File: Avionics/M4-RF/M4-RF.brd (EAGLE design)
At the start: 50.8 x 50.5 mm, 25 parts, among them J1 132134RP, U1 CC1120, U2 CC1190, U3 CC2520, U4 CC2592, U5 INF-PG-LQFP-100-11-7000X7000E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

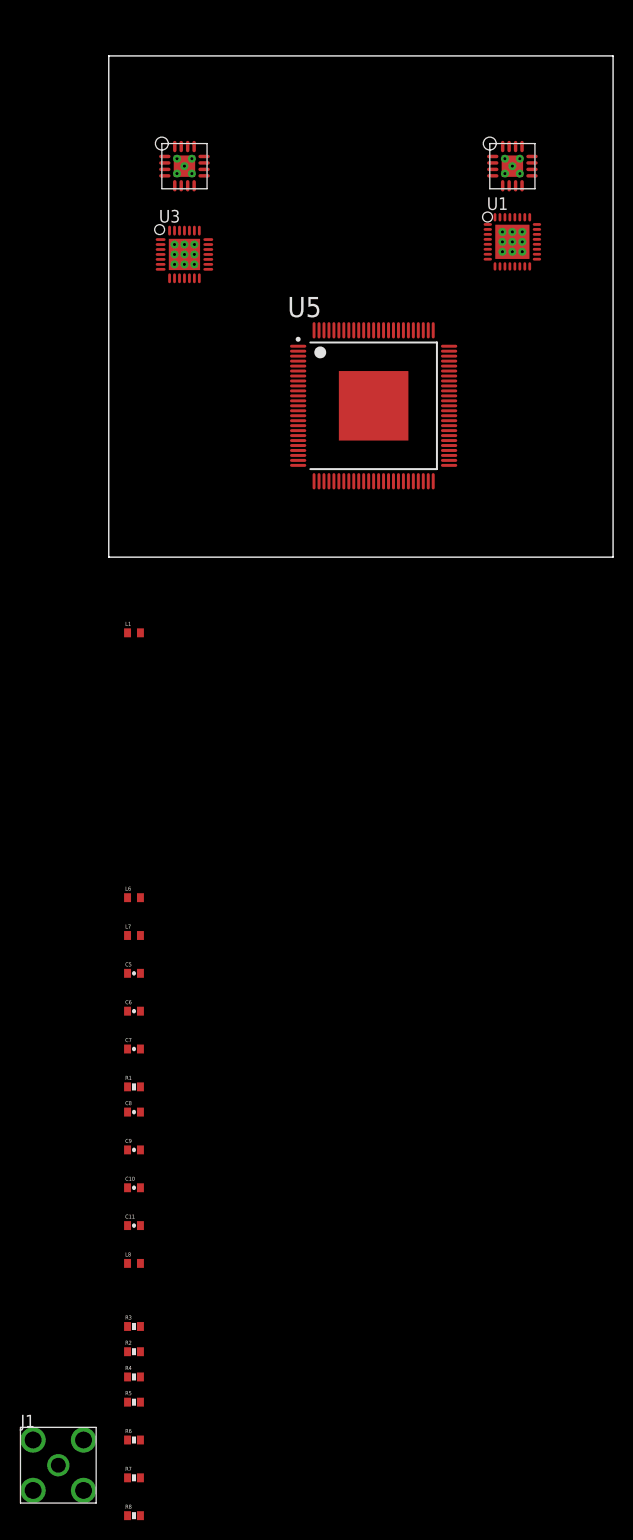
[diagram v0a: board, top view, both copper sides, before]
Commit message: Fixed library references and added balun to 2.4GHz circuit
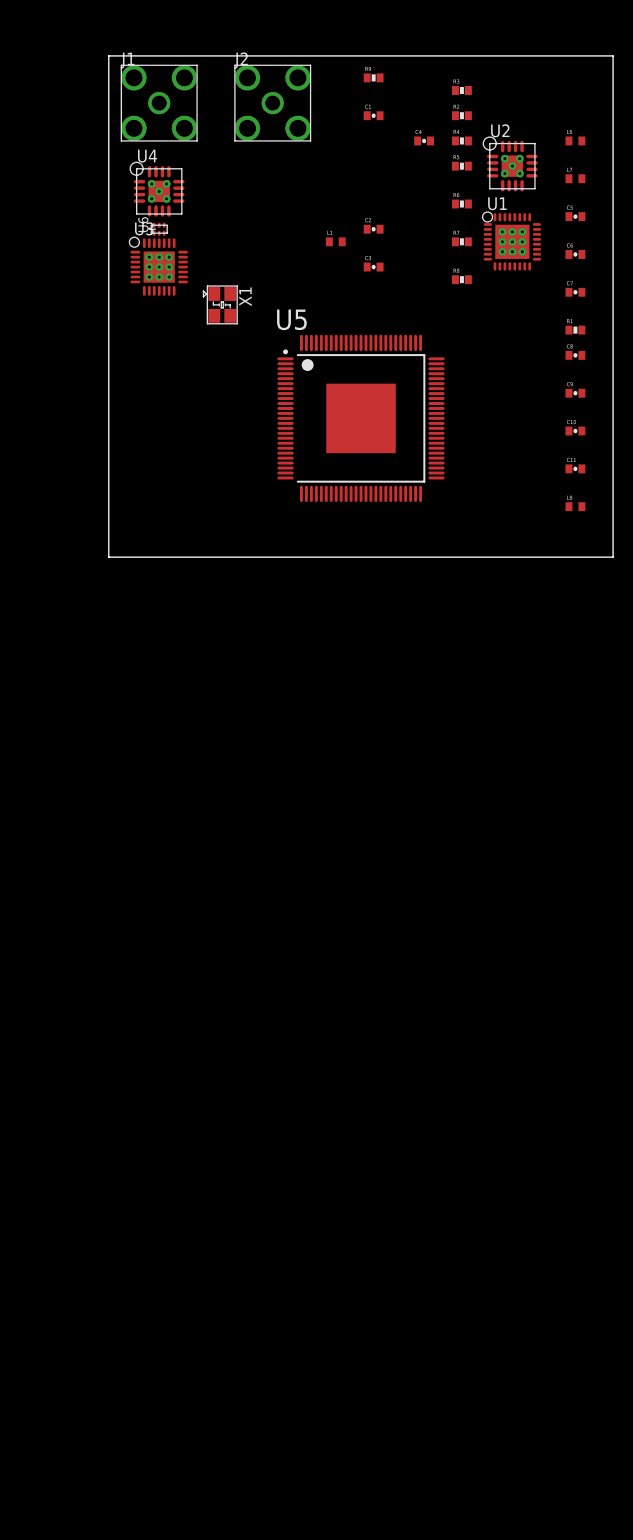
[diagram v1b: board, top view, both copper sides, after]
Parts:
- added C1: 0.1u, SparkFun-Capacitors:0402-CAP
- added C2, C3: 12p, SparkFun-Capacitors:0402-CAP
- added C4: 6.8p, SparkFun-Capacitors:0402-CAP
- added J2: 132134RP, connectors:RP-SMA-TH
- added R9: 56k, SparkFun-Resistors:0402-RES
- added U6: LDB182G4520C-110, rf:LDB18
- added X1: NX3225SA-32MHZ-EXS00A-CS0236832MHZ, oscillators:OSC-4-SMD-3.2MMX2.5MM
- U1: device ti_rf:RHB_S-PVQFN-N32 -> rf:RHB_S-PVQFN-N32
- U2, U4: device ti_rf:RGV_S-PVGFN-N16 -> rf:RGV_S-PVQFN-N16
- U3: device ti_rf:RHD_S-PVQFN-N28 -> rf:RHD_S-PVQFN-N28
- moved J1 137.5 mm to (5.08, 45.7)
- moved R2 128.8 mm to (35.6, 44.5)
- moved R3 128.8 mm to (35.6, 47.0)
- moved R4 128.8 mm to (35.6, 41.9)
- moved R5 128.8 mm to (35.6, 39.4)
- moved R6 128.8 mm to (35.6, 35.6)
- moved R7 128.8 mm to (35.6, 31.8)
- moved R8 128.8 mm to (35.6, 27.9)
- moved C10 88.2 mm to (47.0, 12.7)
- moved C11 88.2 mm to (47.0, 8.89)
- moved C6 88.2 mm to (47.0, 30.5)
- moved C7 88.2 mm to (47.0, 26.7)
- moved C8 88.2 mm to (47.0, 20.3)
- moved C9 88.2 mm to (47.0, 16.5)
- moved L7 88.2 mm to (47.0, 38.1)
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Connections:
- net N$12 renamed 2G4_HG
- new net 2G4_LP: J2.P$1
- new net N$14: U3.11, U3.14, U3.16, U3.20, U3.22, U3.24, U3.8
- new net N$15: C2.2, U3.12, X1.1
- new net N$16: R9.1, U3.23
- new net N$17: C1.2, U3.27
- new net N$18: C3.2, U3.13, X1.3
- new net N$19: R4.1, U6.4
- new net N$20: R5.2, U6.6
- new net N$21: U6.1
- new net N$22: C4.1, U6.3
- net GND: now also C1.1, C2.1, C3.1, C4.2, J2.M1, J2.M2, J2.M3, J2.M4, R9.2, U3.4, U3.EXP@10, U3.EXP@11, X1.2, X1.4

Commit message: Applied DRU
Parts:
- removed J2: 132134RP, connectors:RP-SMA-TH
- added R10: DNP, SparkFun-Resistors:0402-RES
- moved R3 31.6 mm to (8.13, 31.2), turned to 90 degrees
- moved R5 29.8 mm to (6.86, 31.2), turned to 90 degrees
- moved R2 29.1 mm to (9.65, 31.2), turned to 90 degrees
- moved R4 26.8 mm to (10.9, 31.2), turned to 270 degrees
- moved R9 14.5 mm to (23.9, 34.0)
- moved L1 14.0 mm to (8.89, 33.0)
- moved X1 4.38 mm to (12.2, 21.1), turned to 0 degrees
- moved U4 3.81 mm to (8.89, 36.8), turned to 90 degrees
- moved U5 3.81 mm to (25.4, 10.2)
- moved U3 3.54 mm to (6.35, 25.9)
- moved U6 0.76 mm to (5.08, 33.8), flipped to the bottom, turned to 270 degrees
- moved J1 0.25 mm to (4.83, 45.7)
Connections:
- removed net N$21: U6.1
- net 2G4_HG: now also R10.2
- net 2G4_LP: now also R10.1, U6.1; no longer J2.P$1
- net GND: now also U1.EP, U1.EXP@1, U1.EXP@2, U1.EXP@3, U1.EXP@4, U1.EXP@5, U1.EXP@6, U1.EXP@7, U1.EXP@8, U1.EXP@9, U2.1, U2.12, U2.3, U2.9, U2.EP, U2.EP@1, U2.EP@2, U2.EP@3, U2.EP@4, U2.EP@5; no longer J2.M1, J2.M2, J2.M3, J2.M4, U3.EXP@10, U3.EXP@11

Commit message: Added more updates to board layout.
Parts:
- removed L1: DNP, SparkFun-Passives:C0402
- removed R4, R5: DNP, SparkFun-Resistors:0402-RES
- R2: value 0 -> RESISTOR-3PIN-LH-0402; device SparkFun-Resistors:0402-RES -> SparkFun-Resistors:0402-RES-3PIN-LH
- R3: value 0 -> RESISTOR-3PIN-RH-0402; device SparkFun-Resistors:0402-RES -> SparkFun-Resistors:0402-RES-3PIN-RH
- X1: value NX3225SA-32MHZ-EXS00A-CS0236832MHZ -> FA-20H32.0000MF20X-K3; device oscillators:OSC-4-SMD-3.2MMX2.5MM -> oscillators:FA-20H
- moved L8 49.0 mm to (10.9, 38.2), turned to 270 degrees
- moved C6 43.7 mm to (4.50, 40.6), turned to 90 degrees
- moved C11 41.8 mm to (14.9, 35.7), turned to 90 degrees
- moved C5 41.7 mm to (5.59, 39.3), turned to 90 degrees
- moved C10 40.7 mm to (13.4, 35.8), turned to 90 degrees
- moved C8 40.4 mm to (12.0, 40.6), turned to 270 degrees
- moved C7 40.2 mm to (8.78, 39.3), turned to 270 degrees
- moved C9 40.0 mm to (11.9, 35.8), turned to 90 degrees
- moved L7 39.8 mm to (7.19, 40.0), turned to 180 degrees
- moved L6 36.6 mm to (10.4, 39.9), turned to 180 degrees
- moved X1 25.7 mm to (22.9, 44.5), turned to 180 degrees
- moved U3 22.0 mm to (23.6, 39.5), turned to 180 degrees
- moved C3 16.4 mm to (20.4, 44.4), turned to 270 degrees
- moved U6 14.4 mm to (18.2, 39.6), turned to 180 degrees
- moved C4 13.9 mm to (17.9, 41.9), flipped to the bottom, turned to 90 degrees
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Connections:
- removed net N$4: L1.1, R3.2, U4.2
- new net N$12: R3.1, U4.2
- net N$1: now also R3.2; no longer R3.1, R5.1
- net N$19: now also R2.3; no longer R4.1
- net N$2: now also R2.2; no longer R2.1, R4.2
- net N$20: now also R3.3; no longer R5.2
- net N$6: now also R2.1; no longer L1.2, R2.2

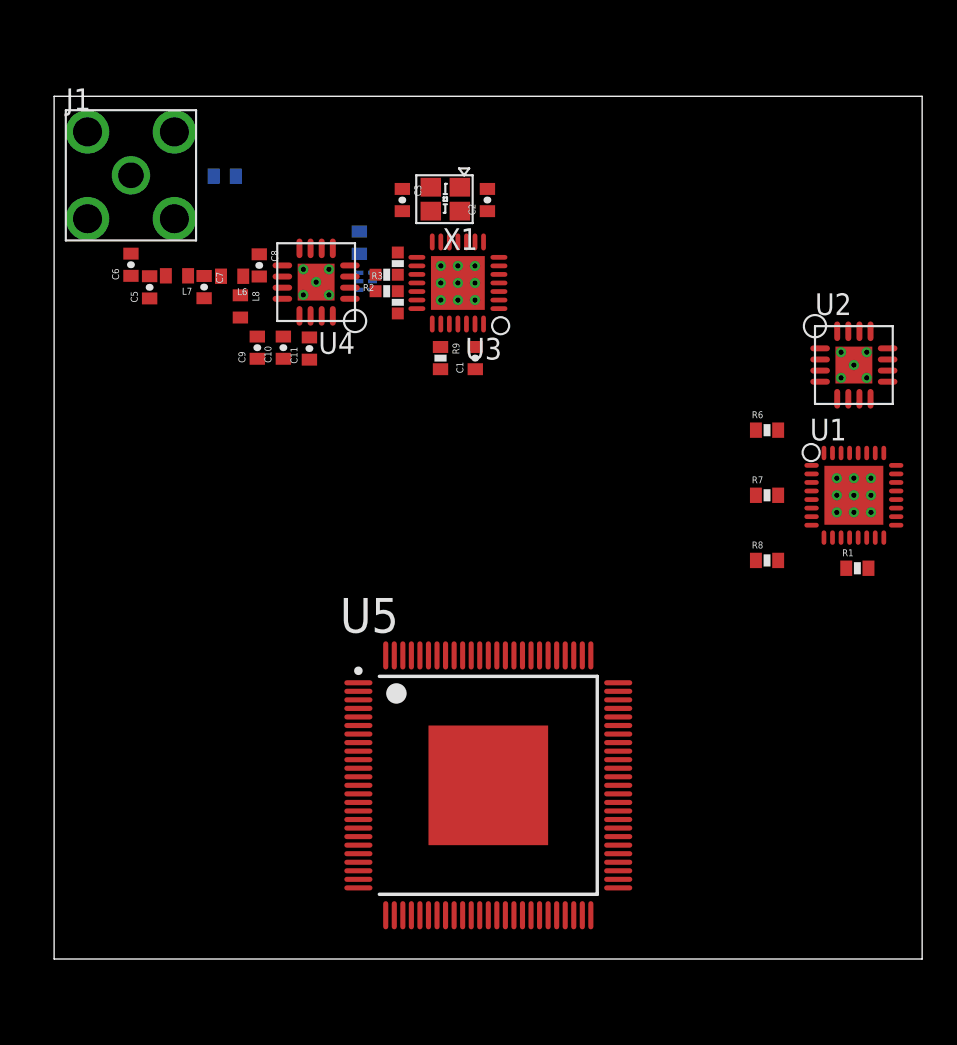
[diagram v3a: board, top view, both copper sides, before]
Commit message: Finished first draft of 2.4GHz layout.
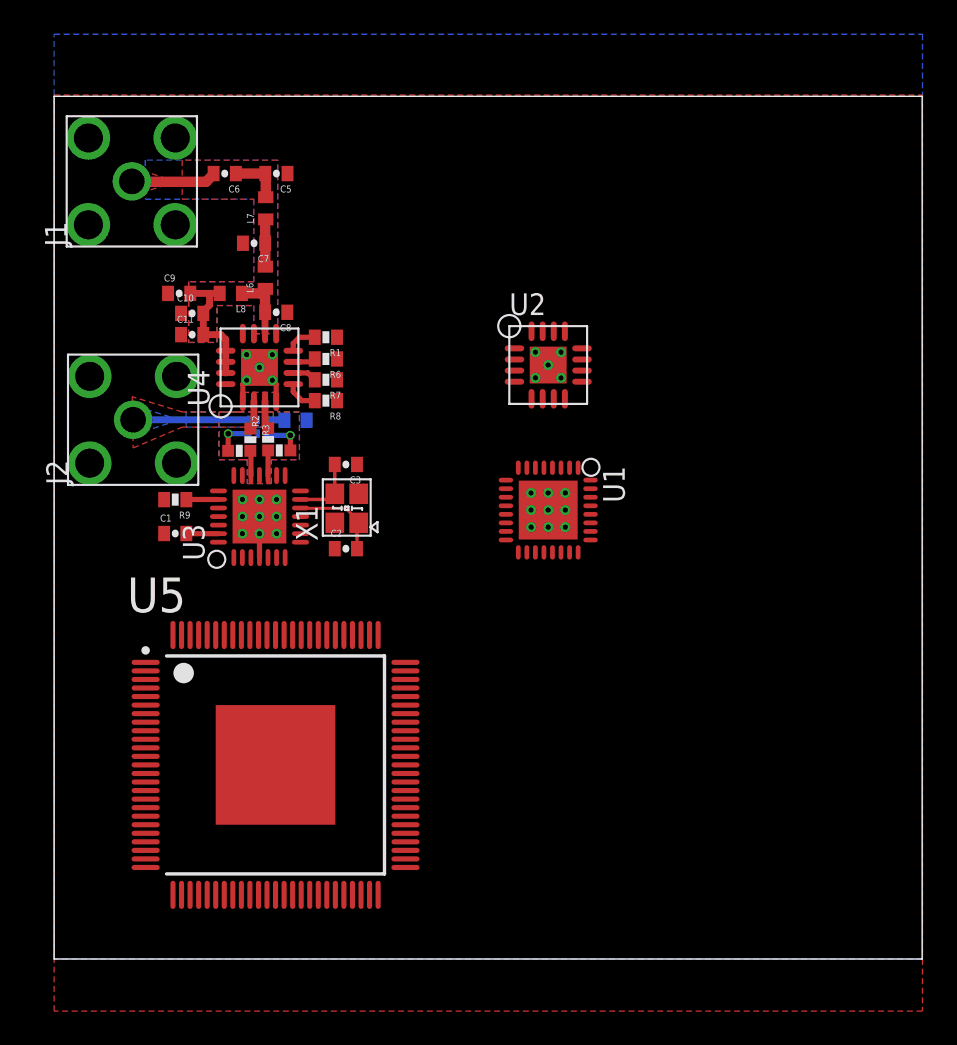
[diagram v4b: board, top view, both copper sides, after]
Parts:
- removed R10: DNP, SparkFun-Resistors:0402-RES
- added J2: 132134RP, connectors:RP-SMA-TH
- moved R1 33.9 mm to (15.9, 36.4), turned to 180 degrees
- moved R8 27.4 mm to (15.9, 32.7), turned to 180 degrees
- moved R7 26.7 mm to (15.9, 33.9), turned to 180 degrees
- moved R6 26.1 mm to (15.9, 35.1), turned to 180 degrees
- moved C2 22.0 mm to (17.1, 24.0), turned to 0 degrees
- moved C1 20.3 mm to (7.09, 24.9), turned to 0 degrees
- moved X1 19.0 mm to (17.1, 26.4), turned to 90 degrees
- moved U3 17.9 mm to (12.0, 25.9), turned to 90 degrees
- moved U1 17.9 mm to (28.9, 26.3), turned to 270 degrees
- moved U2 17.9 mm to (28.9, 34.7)
- moved R9 17.6 mm to (7.09, 26.9), turned to 180 degrees
- moved C3 15.8 mm to (17.1, 28.9), turned to 180 degrees
- moved U5 12.5 mm to (13.0, 11.4)
- moved R2 11.9 mm to (12.5, 30.4), turned to 270 degrees
- moved R3 11.8 mm to (11.5, 30.4), turned to 270 degrees
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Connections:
- removed net 2G4_HG: C6.2, J1.P$1, R10.2
- new net 2G4_LG: C6.2, J1.P$1
- net 2G4_LP: now also J2.P$1; no longer R10.1
- net GND: now also J2.M1, J2.M2, J2.M3, J2.M4
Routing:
- net N$10: track 0.00 -> 7.67 mm
- net 2G4_LP: track 0.00 -> 6.79 mm
- net N$15: track 0.00 -> 5.40 mm
- net 2G4_LG: track 0.00 -> 5.02 mm
- net N$7: track 0.00 -> 4.11 mm
- net GND: track 0.00 -> 4.04 mm
- net N$18: track 0.00 -> 3.85 mm
- net N$9: track 0.00 -> 3.12 mm
- net N$8: track 0.00 -> 2.78 mm
- net N$19: track 0.00 -> 2.32 mm, vias 0 -> 1
- net N$20: track 0.00 -> 2.24 mm, vias 0 -> 1
- net N$13: track 0.00 -> 1.93 mm
- net N$17: track 0.00 -> 1.88 mm
- net N$16: track 0.00 -> 1.88 mm
- net N$11: track 0.00 -> 1.84 mm
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- added copper zone on layer 1, net 2G4_LG
- added copper zone on layer 16, net 2G4_LP
- added copper zone on layer 1, net GND
- added copper zone on layer 15, net GND
- added copper zone on layer 16, net GND
- added copper zone on layer 2, net GND
- added copper zone on layer 1, net N$21
- added copper zone on layer 15, net N$21
- added copper zone on layer 16, net N$21
- added copper zone on layer 2, net N$21
- added copper zone on layer 1, net N$4
- added copper zone on layer 15, net N$4
- added copper zone on layer 16, net N$4
- added copper zone on layer 2, net N$4
- added copper zone on layer 1, net RFCUTOUT1
- added copper zone on layer 15, net RFCUTOUT1
- added copper zone on layer 16, net RFCUTOUT1
- added copper zone on layer 2, net RFCUTOUT1

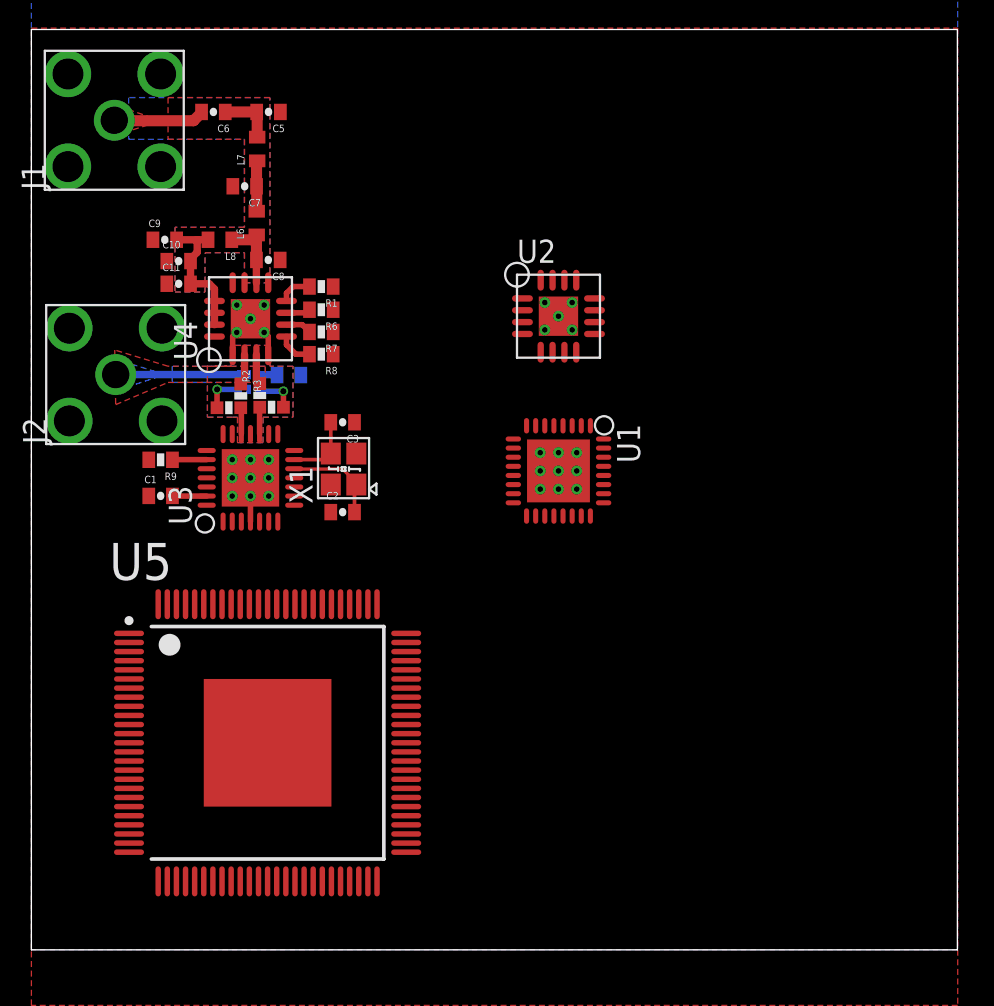
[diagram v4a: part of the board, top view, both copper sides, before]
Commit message: Started to build 900MHz circuit
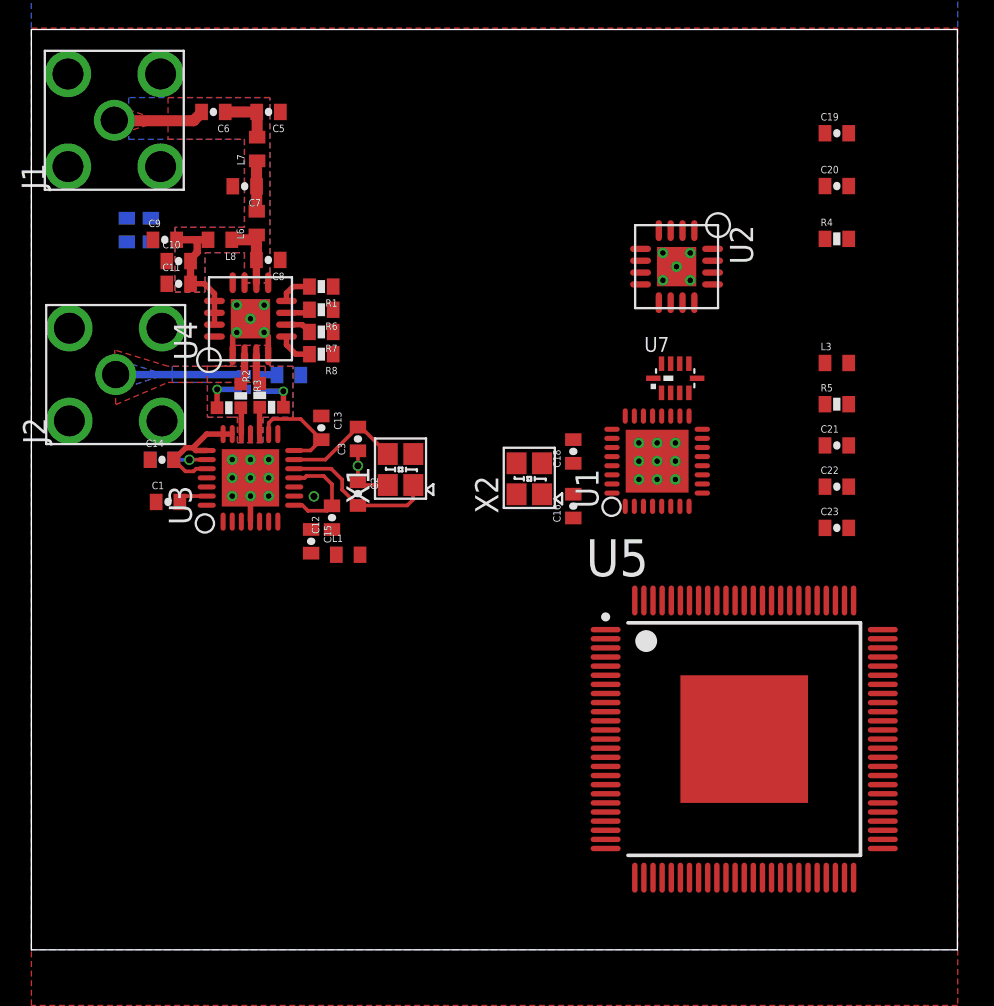
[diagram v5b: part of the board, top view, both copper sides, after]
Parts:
- added C12, C13, C14: 0.1u, SparkFun-Capacitors:0402-CAP
- added C15, C17: 2.2u, SparkFun-Capacitors:0402-CAP
- added C16, C18: 12p, SparkFun-Capacitors:0402-CAP
- added C19: 47n, SparkFun-Capacitors:0402-CAP
- added C20: 220n, SparkFun-Capacitors:0402-CAP
- added C21: 33p, SparkFun-Passives:0402-CAP
- added C22: 10n, SparkFun-Passives:0402-CAP
- added C23: 100p, SparkFun-Passives:0402-CAP
- added L1, L2: BEAD 100, SparkFun-Passives:C0402
- added L3: 10n, SparkFun-Passives:C0402
- added R4: 56k, SparkFun-Resistors:0402-RES
- added R5: 15, SparkFun-Resistors:0402-RES
- added U7: 0900PC15J0013, rf:0900PC15J0013
- added X2: FA-20H32.0000MF20X-K3, oscillators:FA-20H
- moved U5 26.1 mm to (39.1, 11.6)
- moved U2 7.02 mm to (35.4, 37.5), turned to 270 degrees
- moved U1 5.44 mm to (34.3, 26.8), turned to 90 degrees
- moved X1 3.12 mm to (20.2, 26.3)
- moved C2 1.32 mm to (17.9, 25.0), turned to 270 degrees
- moved C3 1.24 mm to (17.9, 28.0), turned to 90 degrees
- moved C1 0.52 mm to (7.49, 24.6)
- moved R9 0.08 mm to (7.16, 26.9), flipped to the bottom, turned to 0 degrees
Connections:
- new net 2G2_SFD: U3.5
- new net 2G4_CCA: U3.6
- new net 2G4_CS_L: U3.3
- new net 2G4_FIFO: U3.9
- new net 2G4_FIFOP: U3.7
- new net 2G4_HGM: R6.1
- new net 2G4_LNA_EN: R7.1
- new net 2G4_PA_EN: R8.1
- new net 2G4_RESET_L: U3.25
- new net 2G4_SCLK: U3.28
- new net 2G4_SI: U3.2
- new net 2G4_SO: U3.1
- new net 2G4_VREG_EN: U3.26
- new net N$24: C16.2, U1.31, X2.1
- new net N$25: C18.2, U1.30, X2.3
- new net N$26: C19.2, U1.29
- new net N$27: C20.2, U1.6
- new net N$28: R4.2, U1.14
- new net N$29: U1.20, U7.1
- new net N$30: U1.19, U7.2
- new net N$31: U1.18, U7.3
- new net N$32: L3.1, U1.17, U7.4
- new net N$33: C21.1, L3.2, R5.2
- new net VDD_CC1120: C21.2, C22.1, C23.1, R5.1
- new net VDD_CC2520: L1.2
- new net VDD_CC2592: L2.2
- net GND: now also C12.1, C13.1, C14.1, C15.1, C16.1, C17.1, C18.1, C19.1, C20.1, C22.2, C23.2, R4.1, U7.10, U7.5, U7.6, U7.8, U7.9, X2.2, X2.4
- net N$10: now also C17.2, L2.1
- net N$14: now also C12.2, C13.2, C14.2, C15.2, L1.1
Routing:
- net N$14: track 0.00 -> 18.3 mm
- net GND: track 4.04 -> 7.44 mm, vias 0 -> 1
- net N$15: track 5.40 -> 8.61 mm
- net N$18: track 3.85 -> 6.48 mm
- net N$16: track 1.88 -> 1.80 mm, vias 0 -> 1
- removed copper zone on layer 2, net GND
